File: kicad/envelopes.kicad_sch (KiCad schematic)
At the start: 47 parts, among them Q1 BC556, Q10 BC546, Q11 BC546, Q12 BC546, Q15 BC546, Q16 BC546, Q2 BC546, Q3 BC546, Q5 BC556, Q7 BC546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

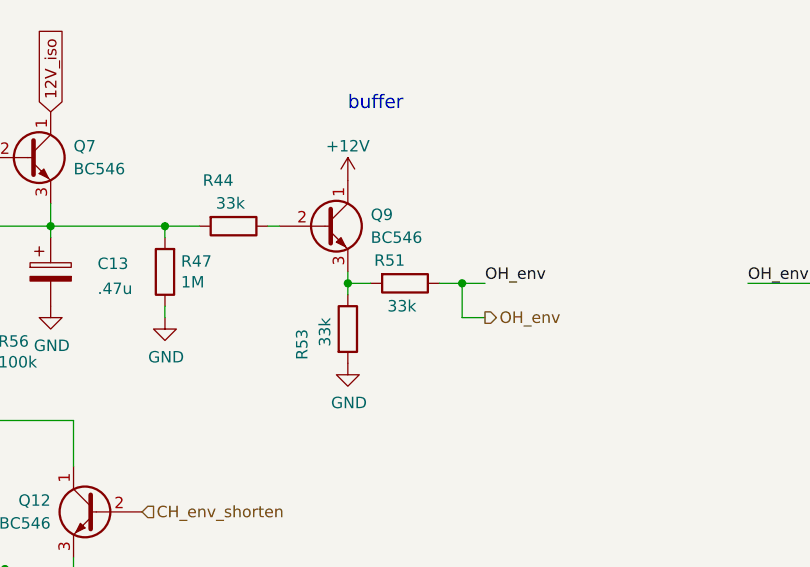
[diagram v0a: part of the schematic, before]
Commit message: remove R51, now the open hat is much louder!
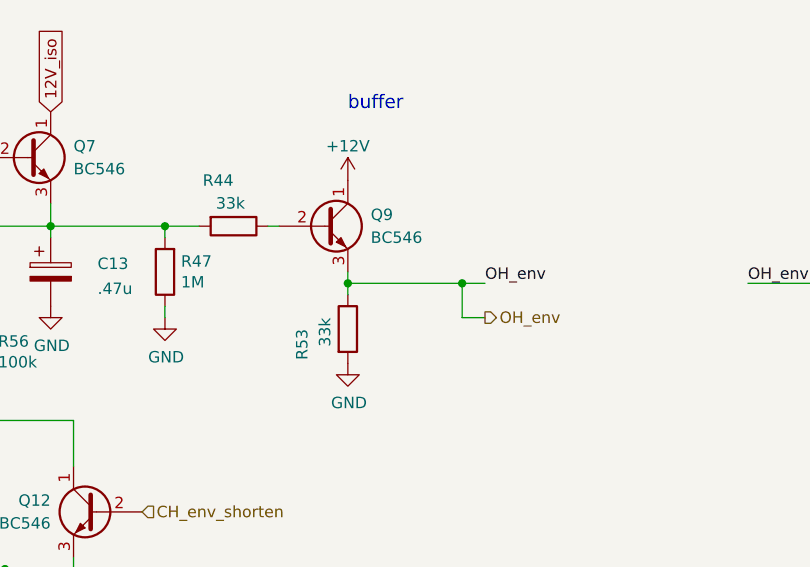
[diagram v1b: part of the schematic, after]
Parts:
- removed R51: 33k, ao_tht:R_Axial_DIN0207_L6.3mm_D2.5mm_P10.16mm_Horizontal, symbol ao_symbols:R
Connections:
- net OH_env: now also Q9.3 (E), R53.1
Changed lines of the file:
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@@
     (stroke (width 0) (type default) (color 0 0 0 0))
   )
-  (wire (pts (xy 175.26 114.3) (xy 177.8 114.3))
+  (wire (pts (xy 175.26 114.3) (xy 187.96 114.3))
     (stroke (width 0) (type default) (color 0 0 0 0))
   )
@@
   )
   (wire (pts (xy 187.96 114.3) (xy 187.96 118.11))
-    (stroke (width 0) (type default) (color 0 0 0 0))
-  )
-  (wire (pts (xy 185.42 114.3) (xy 187.96 114.3))
     (stroke (width 0) (type default) (color 0 0 0 0))
   )
@@
       (effects (font (size 1.27 1.27)) hide)
     )
-    (pin "1")
-    (pin "2")
-  )
-  (symbol (lib_id "ao_symbols:R") (at 181.61 114.3 270) (unit 1)
-    (in_bom yes) (on_board yes)
-    (property "Reference" "R51" (id 0) (at 181.61 111.76 90)
-      (effects (font (size 1.27 1.27)) (justify right))
-    )
-    (property "Value" "33k" (id 1) (at 182.88 116.84 90)
-      (effects (font (size 1.27 1.27)) (justify right))
-    )
-    (property "Footprint" "ao_tht:R_Axial_DIN0207_L6.3mm_D2.5mm_P10.16mm_Horizontal" (id 2) (at 181.61 112.522 90)
-      (effects (font (size 1.27 1.27)) hide)
-    )
-    (property "Datasheet" "" (id 3) (at 181.61 114.3 0)
-      (effects (font (size 1.27 1.27)) hide)
-    )
-    (property "Vendor" "Tayda" (id 4) (at 181.61 114.3 0)
-      (effects (font (size 1.27 1.27)) hide)
-    )
